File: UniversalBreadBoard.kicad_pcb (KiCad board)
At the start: 2 copper layers, 81.3 x 53.3 mm, 80 parts, among them J1 Conn_01x06_Pin, J10 Conn_01x06_Pin, J11 Conn_01x06_Pin, J12 Conn_01x06_Pin, J13 Conn_01x06_Pin, J14 Conn_01x06_Pin, J15 Conn_01x06_Pin, J16 Conn_01x06_Pin, J17 Conn_01x06_Pin, J18 Conn_01x06_Pin, J19 Conn_01x06_Pin, J2 Conn_01x06_Pin, J20 Conn_01x06_Pin, J21 Conn_01x06_Pin, J22 Conn_01x06_Pin, J23 Conn_01x06_Pin, J24 Conn_01x06_Pin, J25 Conn_01x06_Pin, J26 Conn_01x06_Pin, J27 Conn_01x06_Pin, J28 Conn_01x06_Pin, J29 Conn_01x06_Pin, J3 Conn_01x06_Pin, J30 Conn_01x06_Pin, J31 Conn_01x06_Pin, J32 Conn_01x06_Pin, J33 Conn_01x06_Pin, J34 Conn_01x06_Pin, J35 Conn_01x06_Pin, J36 Conn_01x06_Pin, J37 Conn_01x06_Pin, J38 Conn_01x06_Pin, J39 Conn_01x06_Pin, J4 Conn_01x06_Pin, J40 Conn_01x06_Pin, J41 Conn_01x06_Pin, J42 Conn_01x06_Pin, J43 Conn_01x06_Pin, J44 Conn_01x06_Pin, J45 Conn_01x06_Pin, J46 Conn_01x06_Pin, J47 Conn_01x06_Pin, J48 Conn_01x06_Pin, J49 Conn_01x06_Pin, J5 Conn_01x06_Pin, J50 Conn_01x06_Pin, J51 Conn_01x06_Pin, J52 Conn_01x06_Pin, J53 Conn_01x06_Pin, J54 Conn_01x06_Pin, J55 Conn_01x06_Pin, J56 Conn_01x06_Pin, J57 Conn_01x06_Pin, J58 Conn_01x06_Pin, J59 Conn_01x06_Pin, J6 Conn_01x06_Pin, J60 Conn_01x06_Pin, J61 Conn_01x06_Pin, J62 Conn_01x06_Pin, J63 Conn_01x06_Pin, J64 Conn_01x06_Pin, J65 Conn_01x06_Pin, J66 Conn_01x06_Pin, J67 Conn_01x06_Pin, J68 Conn_01x06_Pin, J69 Conn_01x06_Pin, J7 Conn_01x06_Pin, J70 Conn_01x06_Pin, J71 Conn_01x06_Pin, J72 Conn_01x06_Pin, J73 Conn_01x06_Pin, J74 Conn_01x06_Pin, J75 Conn_01x06_Pin, J76 Conn_01x06_Pin, J77 Conn_01x06_Pin, J78 Conn_01x06_Pin, J79 Conn_01x06_Pin, J8 Conn_01x06_Pin, J80 Conn_01x06_Pin, J9 Conn_01x06_Pin

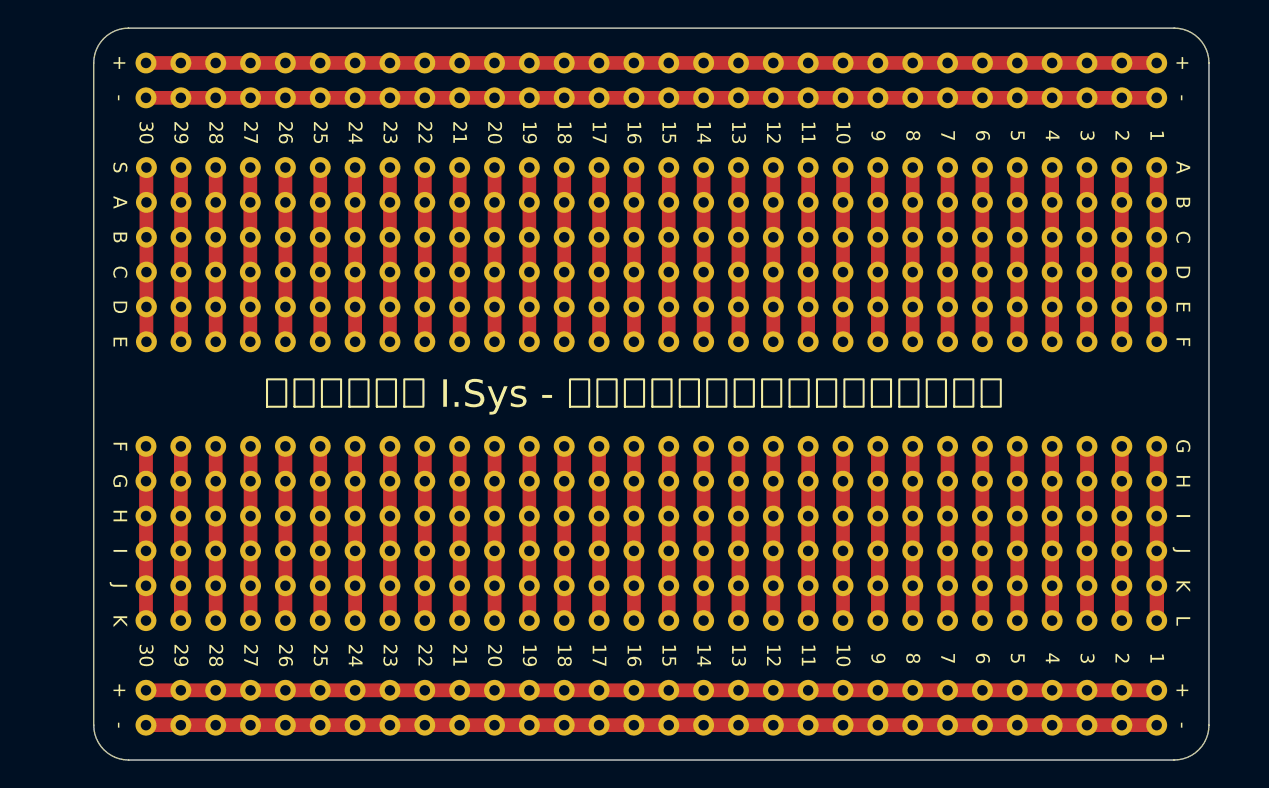
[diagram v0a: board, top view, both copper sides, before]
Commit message: 刻印をオリジナルに変更・リバーシブルに変更
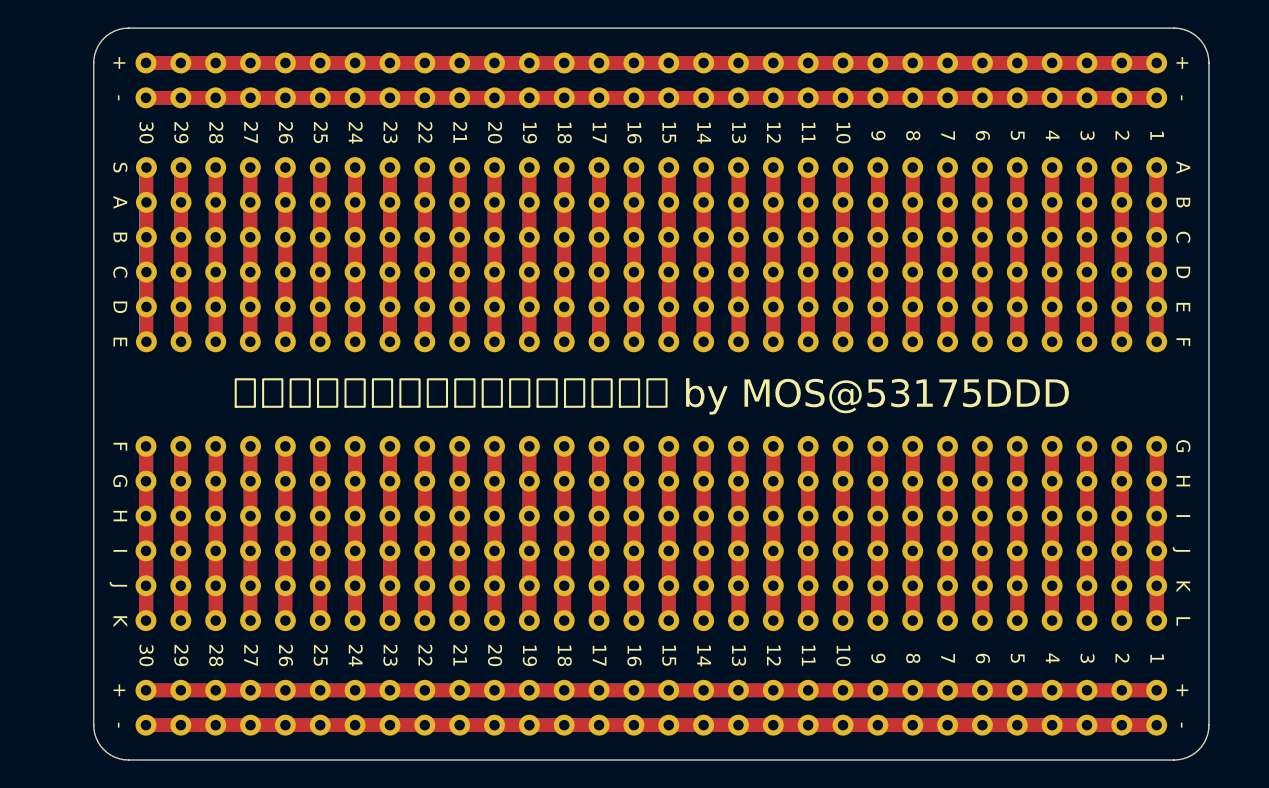
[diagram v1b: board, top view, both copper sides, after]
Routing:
- net Net-(J76-Pin_1): track 73.7 -> 147.3 mm
- net Net-(J71-Pin_1): track 73.7 -> 147.3 mm
- net Net-(J66-Pin_1): track 73.7 -> 147.3 mm
- net Net-(J61-Pin_1): track 73.7 -> 147.3 mm
- net Net-(J9-Pin_1): track 12.7 -> 25.4 mm
- net Net-(J8-Pin_1): track 12.7 -> 25.4 mm
- net Net-(J7-Pin_1): track 12.7 -> 25.4 mm
- net Net-(J6-Pin_1): track 12.7 -> 25.4 mm
- net Net-(J52-Pin_1): track 12.7 -> 25.4 mm
- net Net-(J51-Pin_1): track 12.7 -> 25.4 mm
- net Net-(J50-Pin_1): track 12.7 -> 25.4 mm
- net Net-(J5-Pin_1): track 12.7 -> 25.4 mm
- net Net-(J49-Pin_1): track 12.7 -> 25.4 mm
- net Net-(J4-Pin_1): track 12.7 -> 25.4 mm
- net Net-(J3-Pin_1): track 12.7 -> 25.4 mm
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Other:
- board text added: "ブレッドボード風ユニバーサル基板 by MOS@53175DDD"
- board text removed: "からくり工房 I.Sys - ブレッドボード風ユニバーサル基板"

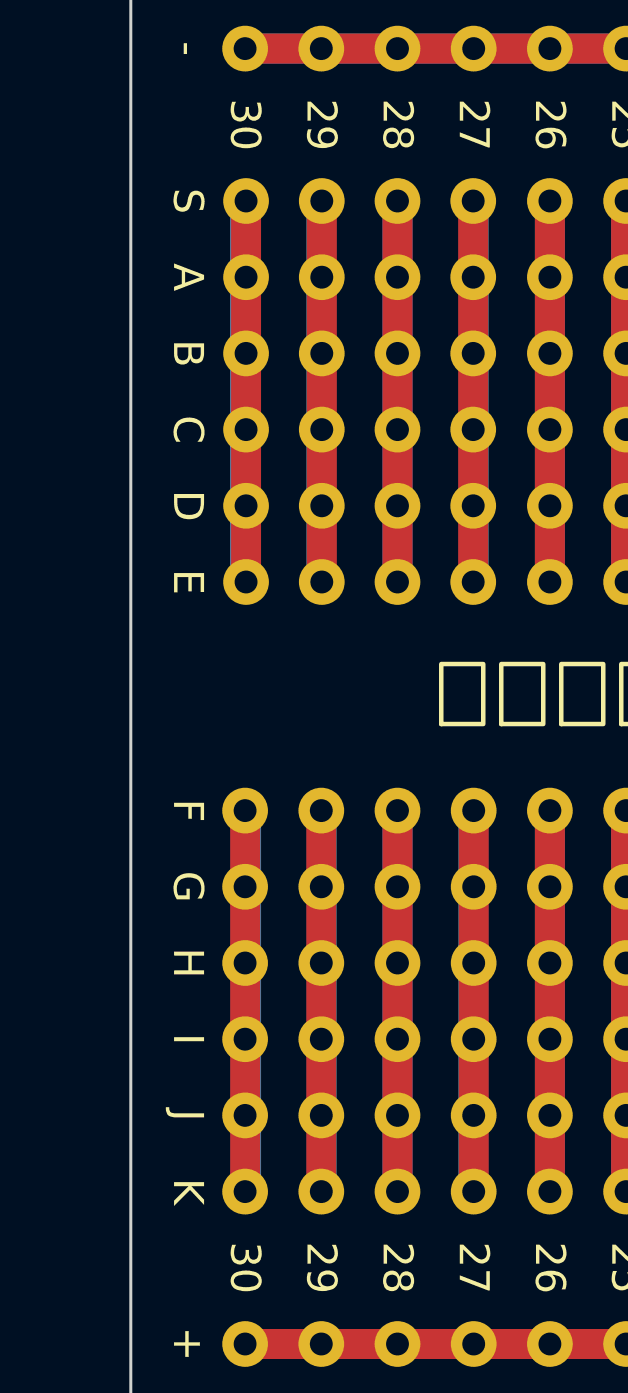
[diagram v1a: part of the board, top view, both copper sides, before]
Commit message: 刻印のミスを修正
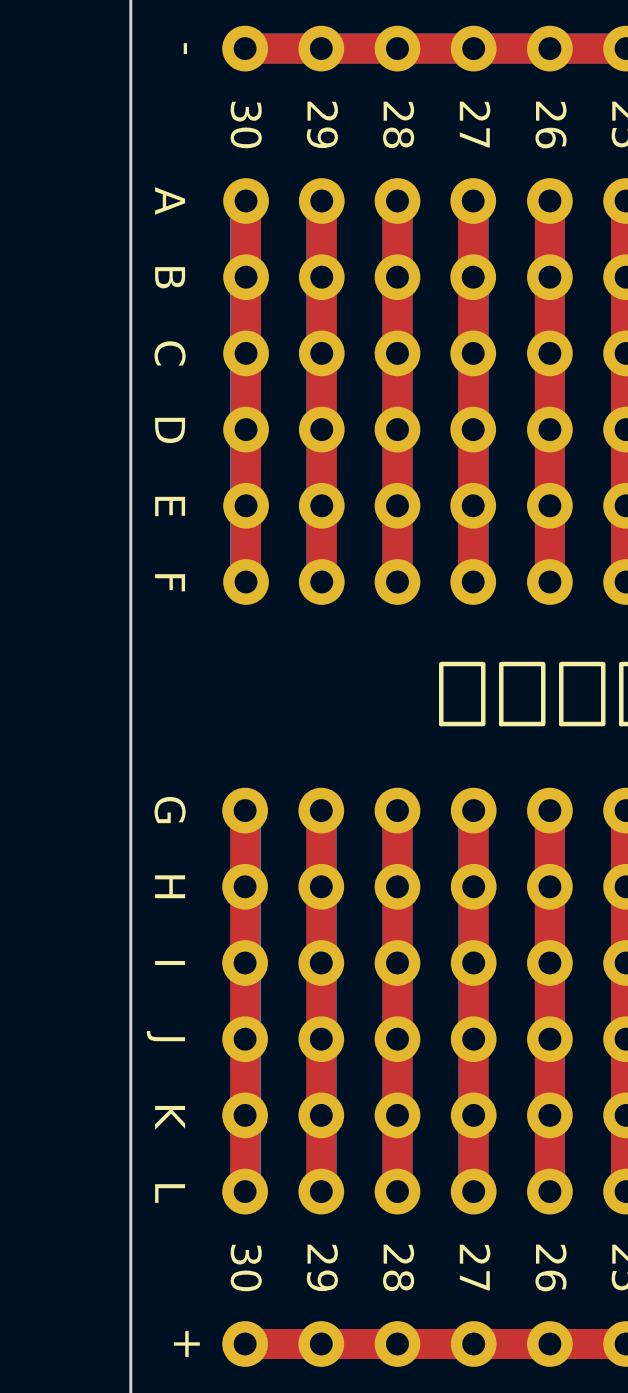
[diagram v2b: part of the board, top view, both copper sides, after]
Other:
- board text removed: "S"
